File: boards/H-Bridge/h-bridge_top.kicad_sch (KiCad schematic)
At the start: 0 parts

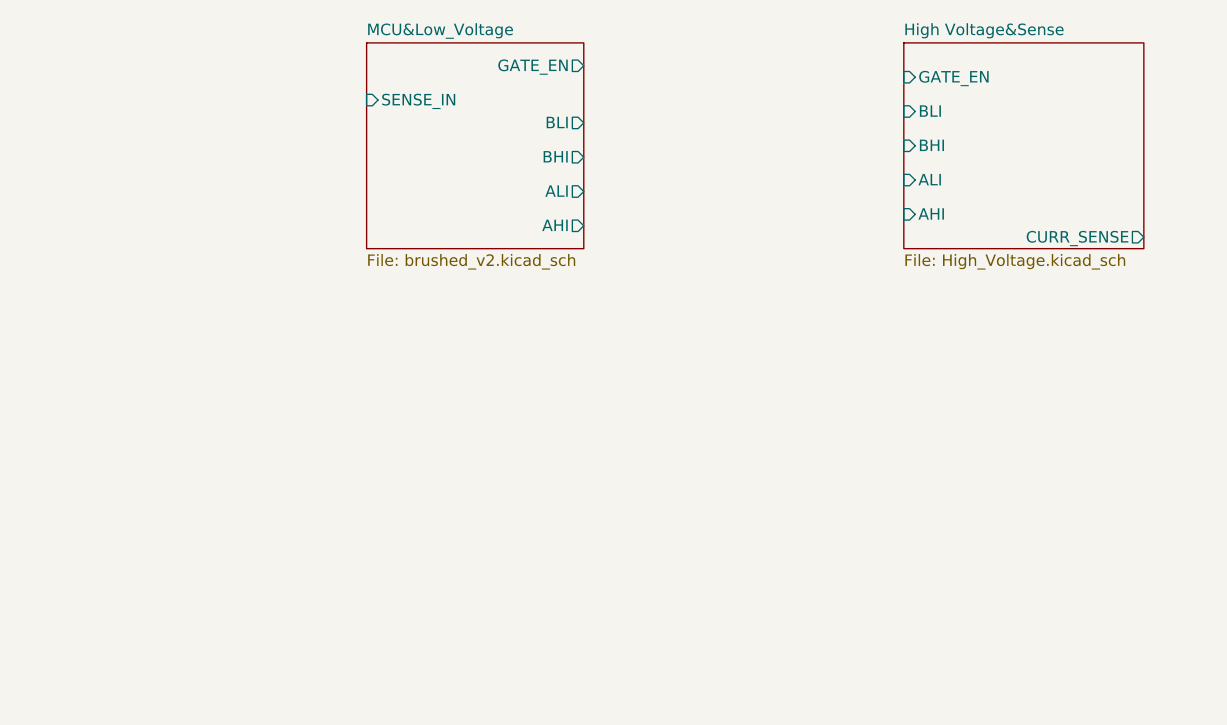
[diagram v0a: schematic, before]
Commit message: finished schematic (i think), added footprints
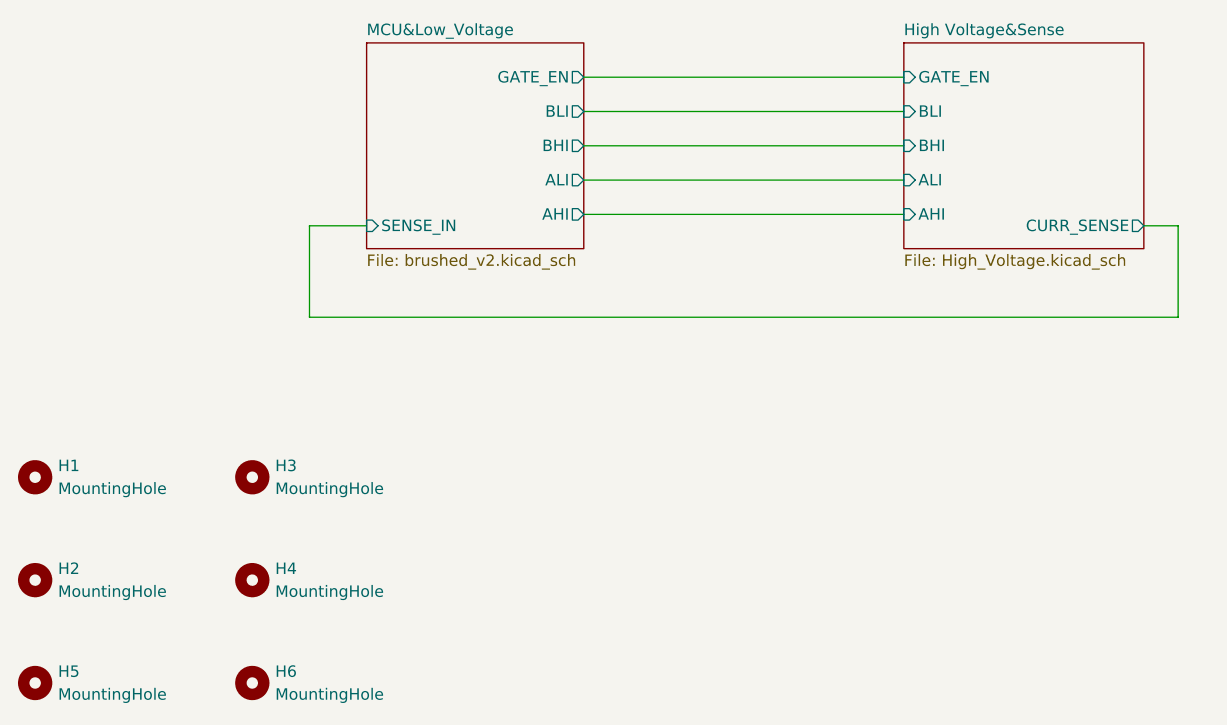
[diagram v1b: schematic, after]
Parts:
- added H1, H2, H3, H4, H5, H6: MountingHole, symbol Mechanical:MountingHole

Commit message: finished schematic, added footprint assignments
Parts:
- H1, H2, H3, H4: footprint (none) -> MountingHole:MountingHole_4.3mm_M4
- H5, H6: footprint (none) -> MountingHole:MountingHole_3mm
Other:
- moved on the sheet: H1, H2, H3, H4, H5, H6
